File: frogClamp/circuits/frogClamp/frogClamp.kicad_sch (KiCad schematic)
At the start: 5 parts

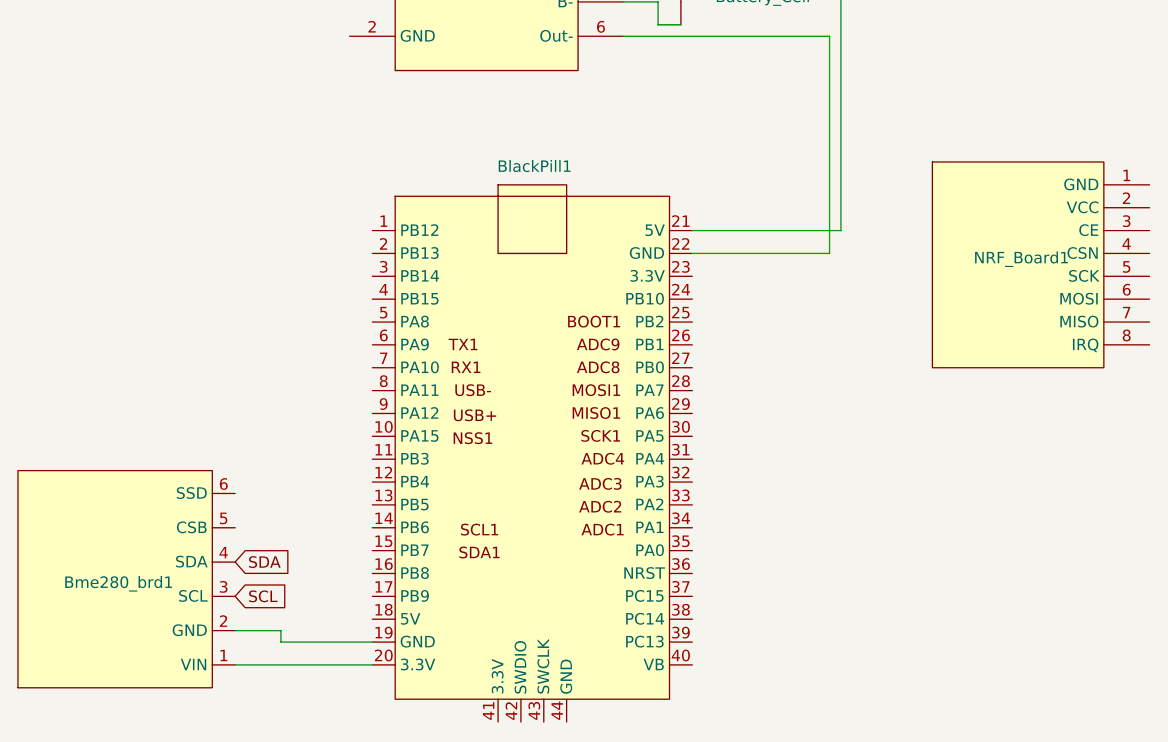
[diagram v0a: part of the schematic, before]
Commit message: Added libraries to project
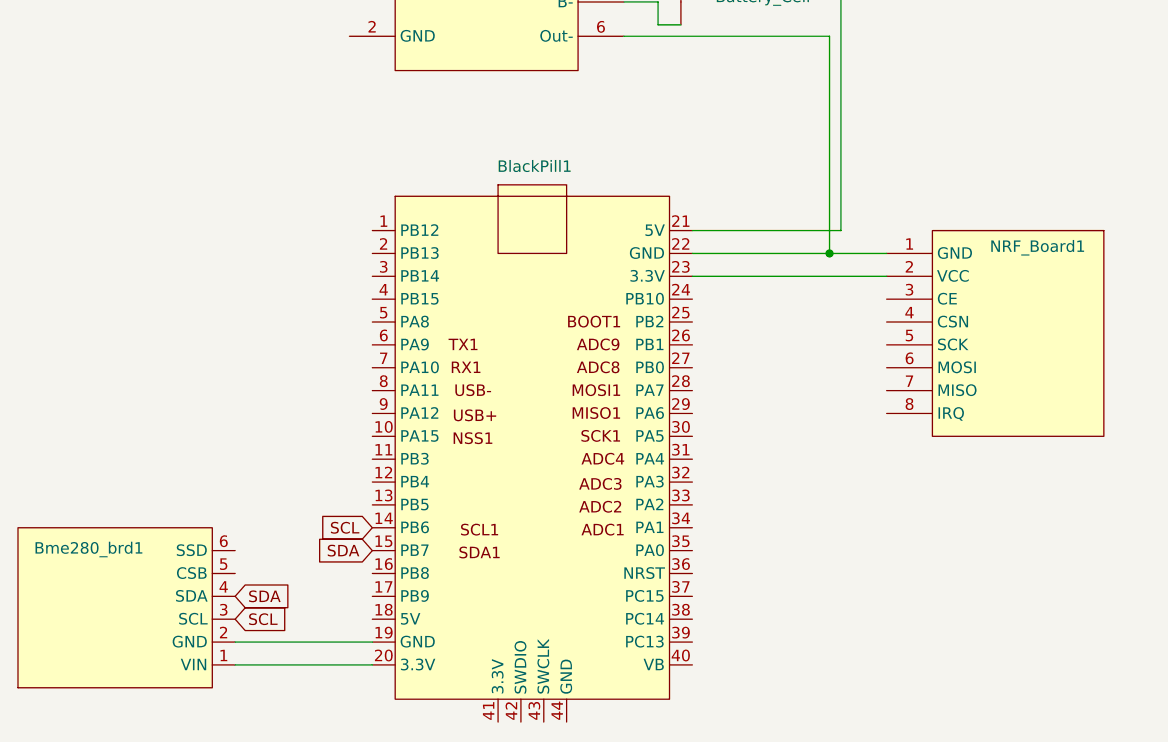
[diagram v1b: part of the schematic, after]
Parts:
- BT1: footprint (none) -> AARobin:Lipo Battery
- BlackPill1: footprint (none) -> AARobin:BlackPill
- Bme280_brd1: footprint (none) -> AARobin:BME280_brd
- RD_TP4046Bat_brd1: footprint (none) -> AARobin:TP4056-18650
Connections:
- net SCL: now also BlackPill1.14 (PB6)
- net SDA: now also BlackPill1.15 (PB7)
- net at BlackPill1.22 (GND), RD_TP4046Bat_brd1.6 (Out-): now also NRF_Board1.1 (GND)
- net at BlackPill1.23 (3.3V): now also NRF_Board1.2 (VCC)
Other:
- moved on the sheet: Bme280_brd1, NRF_Board1
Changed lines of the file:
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@@
 	(generator_version "9.0")
 	(paper "A4")
-	(wire
-		(pts
-			(xy 95.25 113.03) (xy 105.41 113.03)
-		)
-		(stroke
-			(width 0)
-			(type default)
-		)
-	)
-	(wire
-		(pts
-			(xy 90.17 111.76) (xy 95.25 111.76)
+	(junction
+		(at 156.21 69.85)
+		(diameter 0)
+		(color 0 0 0 0)
+	)
+	(wire
+		(pts
+			(xy 90.17 113.03) (xy 105.41 113.03)
 		)
 		(stroke
@@
 	(wire
 		(pts
+			(xy 156.21 69.85) (xy 162.56 69.85)
+		)
+		(stroke
+			(width 0)
+			(type default)
+		)
+	)
+	(wire
+		(pts
 			(xy 137.16 41.91) (xy 137.16 44.45)
 		)
@@
 	(wire
 		(pts
-			(xy 95.25 111.76) (xy 95.25 113.03)
+			(xy 140.97 72.39) (xy 162.56 72.39)
 		)
 		(stroke
@@
 	)
 	(global_label "SCL"
+		(shape input)
+		(at 90.17 110.49 0)
+		(fields_autoplaced yes)
+		(effects
+			(font
+				(size 1.27 1.27)
+			)
+			(justify left)
+		)
+		(property "Intersheetrefs" "${INTERSHEET_REFS}"
+			(at 96.6628 110.49 0)
+			(effects
+				(font
+					(size 1.27 1.27)
+				)
+				(justify left)
+				(hide yes)
+			)
+		)
+	)
+	(global_label "SCL"
+		(shape input)
+		(at 105.41 100.33 180)
+		(fields_autoplaced yes)
+		(effects
+			(font
+				(size 1.27 1.27)
+			)
+			(justify right)
+		)
+		(property "Intersheetrefs" "${INTERSHEET_REFS}"
+			(at 98.9172 100.33 0)
+			(effects
+				(font
+					(size 1.27 1.27)
+				)
+				(justify right)
+				(hide yes)
+			)
+		)
+	)
+	(global_label "SDA"
+		(shape input)
+		(at 105.41 102.87 180)
+		(fields_autoplaced yes)
+		(effects
+			(font
+				(size 1.27 1.27)
+			)
+			(justify right)
+		)
+		(property "Intersheetrefs" "${INTERSHEET_REFS}"
+			(at 98.8567 102.87 0)
+			(effects
+				(font
+					(size 1.27 1.27)
+				)
+				(justify right)
+				(hide yes)
+			)
+		)
+	)
+	(global_label "SDA"
 		(shape input)
 		(at 90.17 107.95 0)
@@
 		)
 		(property "Intersheetrefs" "${INTERSHEET_REFS}"
-			(at 96.6628 107.95 0)
-			(effects
-				(font
-					(size 1.27 1.27)
-				)
-				(justify left)
-				(hide yes)
-			)
-		)
-	)
-	(global_label "SDA"
-		(shape input)
-		(at 90.17 104.14 0)
-		(fields_autoplaced yes)
-		(effects
-			(font
-				(size 1.27 1.27)
-			)
-			(justify left)
-		)
-		(property "Intersheetrefs" "${INTERSHEET_REFS}"
-			(at 96.7233 104.14 0)
+			(at 96.7233 107.95 0)
 			(effects
 				(font
@@
 		(dnp no)
 		(property "Reference" "Bme280_brd1"
-			(at 71.12 106.426 0)
+			(at 67.818 102.616 0)
 			(effects
 				(font
@@
 			)
 		)
-		(property "Footprint" ""
+		(property "Footprint" "AARobin:BME280_brd"
 			(at 80.01 110.49 0)
 			(effects
@@
 			)
 		)
-		(property "Footprint" ""
+		(property "Footprint" "AARobin:BlackPill"
 			(at 123.19 90.17 0)
 			(effects
@@
 	(symbol
 		(lib_id "AARobin:RD_NRF_Board")
-		(at 173.99 71.12 0)
+		(at 180.34 78.74 0)
+		(mirror y)
 		(unit 1)
 		(exclude_from_sim no)
@@
 		(dnp no)
 		(property "Reference" "NRF_Board1"
-			(at 172.212 70.358 0)
+			(at 184.658 69.088 0)
 			(effects
 				(font
@@
 		)
 		(property "Value" "~"
-			(at 193.04 72.39 0)
+			(at 161.29 80.01 0)
 			(effects
 				(font
@@
 		)
 		(property "Footprint" ""
-			(at 173.99 71.12 0)
+			(at 180.34 78.74 0)
 			(effects
 				(font
@@
 		)
 		(property "Datasheet" ""
-			(at 173.99 71.12 0)
+			(at 180.34 78.74 0)
 			(effects
 				(font
@@
 		)
 		(property "Description" ""
-			(at 173.99 71.12 0)
+			(at 180.34 78.74 0)
 			(effects
 				(font
@@
 			)
 		)
-		(property "Footprint" ""
+		(property "Footprint" "AARobin:TP4056-18650"
 			(at 120.65 40.64 0)
 			(effects
@@
 			)
 		)
-		(property "Footprint" ""
+		(property "Footprint" "AARobin:Lipo Battery"
 			(at 139.7 40.386 90)
 			(effects

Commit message: finished schematic, rough board layout
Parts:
- added BZ1: Buzzer, Crystal:Resonator-2Pin_W6.0mm_H3.0mm, symbol Device:Buzzer
- added D1, D2: 1N5407, Diode_SMD:D_1206_3216Metric_Pad1.42x1.75mm_HandSolder, symbol Diode:1N5407
- added M1: Motor Pump, AARobin:miniPump_1.2, symbol Motor:Motor_DC_ALT
- added M2: Solenoid Valve, AARobin:SolenoidValve_9.0, symbol Motor:Motor_DC_ALT
- added Q1, Q2: QM6006D, Package_TO_SOT_SMD:TO-252-2, symbol Transistor_FET:QM6006D
- added R1, R4: 10k, Resistor_SMD:R_1206_3216Metric, symbol Device:R
- added R2, R3: 100, Resistor_SMD:R_1206_3216Metric, symbol Device:R
- added SW1: SW_SPDT, Button_Switch_SMD:SW_SPST_B3U-1100P, symbol Switch:SW_SPDT
- NRF_Board1: footprint (none) -> AARobin:nRF24L01_Breakout
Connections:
- net 3.3V: now reaches BlackPill1.20 (3.3V), Bme280_brd1.1 (VIN)
- net 3.3V: now also BlackPill1.23 (3.3V), NRF_Board1.2 (VCC), D1.1 (K), D2.1 (K), M1.1 (+), M2.1 (+)
- net GND: now reaches BlackPill1.19 (GND), Bme280_brd1.2 (GND)
- net GND: now also BlackPill1.22 (GND), NRF_Board1.1 (GND), RD_TP4046Bat_brd1.6 (Out-), BZ1.2 (-), Q1.3 (S), Q2.3 (S), R1.2, R4.2
- net NRF_CE: now reaches BlackPill1.1 (PB12)
- net NRF_CE: now also NRF_Board1.3 (CE)
- net NRF_SCK: now reaches BlackPill1.2 (PB13)
- net NRF_SCK: now also BlackPill1.24 (PB10), NRF_Board1.5 (SCK)
- net at BlackPill1.21 (5V): now also SW1.1 (A); no longer RD_TP4046Bat_brd1.3 (Out+)
- net VALVE: now reaches BlackPill1.26 (PB1)
- net VALVE: now also R3.1
- net PUMP: now reaches BlackPill1.27 (PB0)
- net PUMP: now also R2.1
- net SPKR: now reaches BlackPill1.28 (PA7)
- net SPKR: now also BZ1.1 (+)
- net PWR_LED: now reaches BlackPill1.29 (PA6)
- net NRF_MOSI: now reaches BlackPill1.3 (PB14)
- net NRF_MOSI: now also NRF_Board1.6 (MOSI)
- net NRF_MISO: now reaches BlackPill1.4 (PB15)
- net NRF_MISO: now also NRF_Board1.7 (MISO)
- net B+: now reaches BlackPill1.40 (VB)
- net B+: now also BT1.1 (+), RD_TP4046Bat_brd1.4 (B+)
- net NRF_CSN: now reaches NRF_Board1.4 (CSN)
- net B-: now reaches BT1.2 (-), RD_TP4046Bat_brd1.5 (B-)
- new net: D2.2 (A), M2.2 (-), Q2.2 (D)
- new net: Q2.1 (G), R3.2, R4.1
- new net: Q1.1 (G), R1.1, R2.2
- new net: D1.2 (A), M1.2 (-), Q1.2 (D)
- new net OUT+: RD_TP4046Bat_brd1.3 (Out+), SW1.2 (B)
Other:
- note added: "01"
- note added: "Air Pump Motor"
- note added: "Frog Clamp V01"
- note added: "June 5, 2025"
- note added: "Microcontroller"
- note added: "Power"
- note added: "Pressure Sensor"
- note added: "Robin Debreuil"
- note added: "Solenoid Valve"
- note added: "Sound"
- note added: "Wireless Communication"
- moved on the sheet: BT1, BlackPill1, Bme280_brd1, NRF_Board1, RD_TP4046Bat_brd1
